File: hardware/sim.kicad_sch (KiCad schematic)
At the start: 8 parts, among them J14 Conn_01x06, J15 SIM_Card

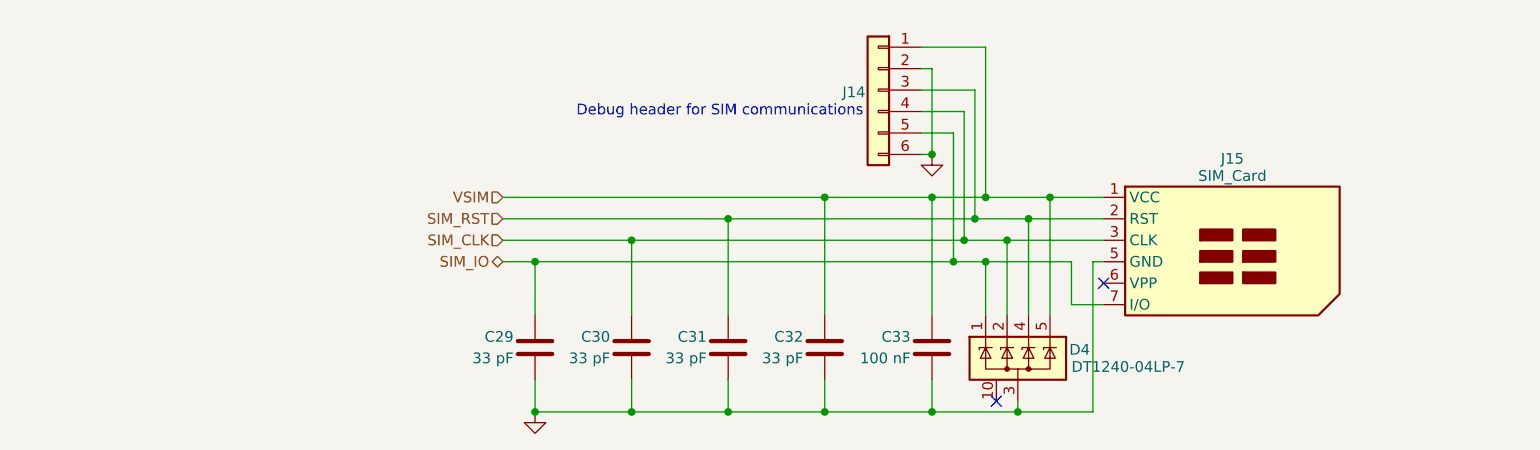
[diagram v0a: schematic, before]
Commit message: HW: Develop further
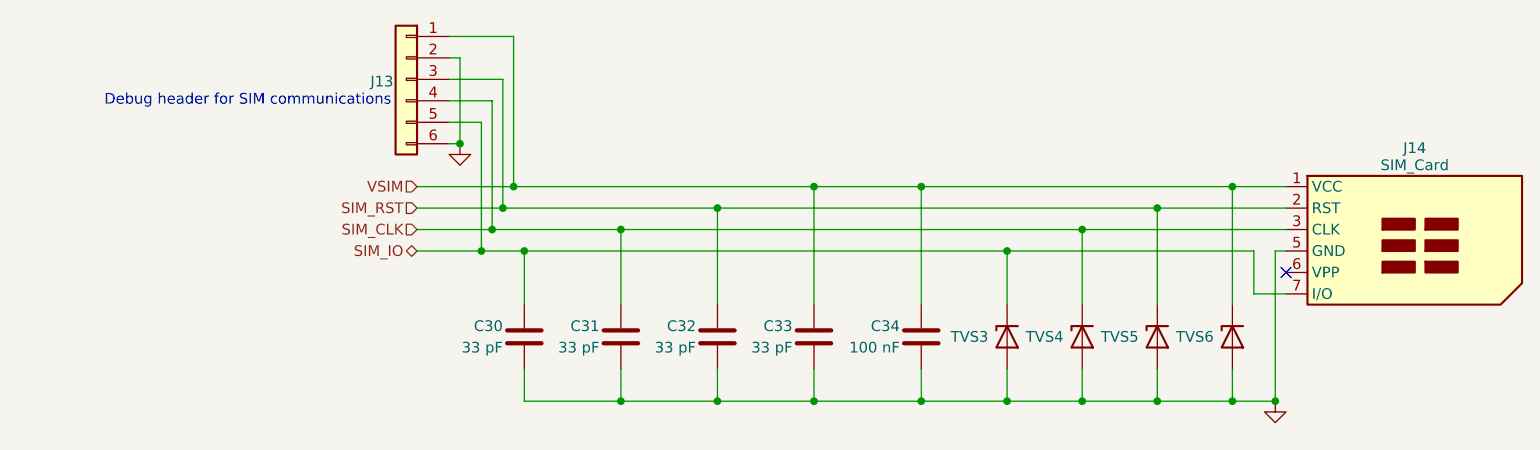
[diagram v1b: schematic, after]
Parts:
- removed D4: DT1240-04LP-7, Package_DFN_QFN:Diodes_UDFN-10_1.0x2.5mm_P0.5mm, symbol DT1240-04LP:DT1240-04LP
- added TVS3, TVS4, TVS5, TVS6: PE1605M1Q_R1_00001, Diode_SMD:D_0402_1005Metric, symbol Device:D_Zener
- renumbered C29 to C30, C30 to C31, C31 to C32, C32 to C33, C33 to C34, J14 to J13, J15 to J14
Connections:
- net GND: now also TVS3.2 (A), TVS4.2 (A), TVS5.2 (A), TVS6.2 (A)
- net SIM_CLK: now also TVS4.1 (K)
- net SIM_IO: now also TVS3.1 (K)
- net SIM_RST: now also TVS5.1 (K)
- net VSIM: now also TVS6.1 (K)
- no-connect marks 2 -> 1
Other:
- moved on the sheet: C30, C31, C32, C33, C34, J13, J14

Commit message: HW: Layout SIM section
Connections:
- net GND: now also J13.5 (Pin_5); no longer J13.6 (Pin_6)
- net SIM_CLK: now also J13.6 (Pin_6); no longer J13.4 (Pin_4)
- net SIM_IO: now also J13.4 (Pin_4); no longer J13.5 (Pin_5)
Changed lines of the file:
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@@
 	)
 	(junction
+		(at 92.71 111.76)
+		(diameter 0)
+		(color 0 0 0 0)
+	)
+	(junction
 		(at 146.05 144.78)
 		(diameter 0)
@@
 	)
 	(junction
-		(at 110.49 144.78)
+		(at 99.06 144.78)
 		(diameter 0)
 		(color 0 0 0 0)
 	)
 	(junction
-		(at 156.21 127)
+		(at 110.49 144.78)
 		(diameter 0)
 		(color 0 0 0 0)
 	)
 	(junction
-		(at 93.98 127)
+		(at 156.21 127)
 		(diameter 0)
 		(color 0 0 0 0)
@@
 	)
 	(junction
-		(at 96.52 121.92)
+		(at 182.88 144.78)
 		(diameter 0)
 		(color 0 0 0 0)
 	)
 	(junction
-		(at 91.44 114.3)
+		(at 97.79 121.92)
 		(diameter 0)
 		(color 0 0 0 0)
 	)
 	(junction
-		(at 182.88 144.78)
+		(at 100.33 119.38)
 		(diameter 0)
 		(color 0 0 0 0)
 	)
 	(junction
-		(at 133.35 144.78)
+		(at 95.25 127)
 		(diameter 0)
 		(color 0 0 0 0)
 	)
 	(junction
-		(at 182.88 119.38)
+		(at 133.35 144.78)
 		(diameter 0)
 		(color 0 0 0 0)
 	)
 	(junction
-		(at 95.25 124.46)
+		(at 182.88 119.38)
 		(diameter 0)
 		(color 0 0 0 0)
 	)
 	(junction
-		(at 97.79 119.38)
+		(at 90.17 124.46)
 		(diameter 0)
 		(color 0 0 0 0)
@@
 	(wire
 		(pts
-			(xy 121.92 121.92) (xy 173.99 121.92)
+			(xy 97.79 106.68) (xy 97.79 121.92)
 		)
 		(stroke
@@
 	(wire
 		(pts
-			(xy 95.25 109.22) (xy 95.25 124.46)
+			(xy 121.92 121.92) (xy 173.99 121.92)
 		)
 		(stroke
@@
 	(wire
 		(pts
-			(xy 96.52 106.68) (xy 96.52 121.92)
+			(xy 92.71 144.78) (xy 99.06 144.78)
 		)
 		(stroke
@@
 	(wire
 		(pts
-			(xy 91.44 104.14) (xy 91.44 114.3)
+			(xy 90.17 106.68) (xy 97.79 106.68)
 		)
 		(stroke
@@
 	(wire
 		(pts
-			(xy 97.79 119.38) (xy 133.35 119.38)
+			(xy 86.36 127) (xy 95.25 127)
 		)
 		(stroke
@@
 	(wire
 		(pts
+			(xy 90.17 114.3) (xy 90.17 124.46)
+		)
+		(stroke
+			(width 0)
+			(type default)
+		)
+	)
+	(wire
+		(pts
 			(xy 146.05 119.38) (xy 182.88 119.38)
 		)
@@
 	(wire
 		(pts
-			(xy 93.98 111.76) (xy 90.17 111.76)
+			(xy 86.36 119.38) (xy 100.33 119.38)
 		)
 		(stroke
@@
 	(wire
 		(pts
-			(xy 96.52 106.68) (xy 90.17 106.68)
+			(xy 156.21 140.97) (xy 156.21 144.78)
 		)
 		(stroke
@@
 	(wire
 		(pts
-			(xy 156.21 140.97) (xy 156.21 144.78)
+			(xy 173.99 121.92) (xy 189.23 121.92)
 		)
 		(stroke
@@
 	(wire
 		(pts
-			(xy 173.99 121.92) (xy 189.23 121.92)
+			(xy 100.33 101.6) (xy 100.33 119.38)
 		)
 		(stroke
@@
 	(wire
 		(pts
-			(xy 97.79 101.6) (xy 97.79 119.38)
+			(xy 99.06 127) (xy 156.21 127)
 		)
 		(stroke
@@
 	(wire
 		(pts
-			(xy 99.06 127) (xy 156.21 127)
+			(xy 173.99 121.92) (xy 173.99 133.35)
 		)
 		(stroke
@@
 	(wire
 		(pts
-			(xy 173.99 121.92) (xy 173.99 133.35)
+			(xy 182.88 119.38) (xy 189.23 119.38)
 		)
 		(stroke
@@
 	(wire
 		(pts
-			(xy 182.88 119.38) (xy 189.23 119.38)
+			(xy 100.33 119.38) (xy 133.35 119.38)
 		)
 		(stroke
@@
 	(wire
 		(pts
-			(xy 99.06 140.97) (xy 99.06 144.78)
+			(xy 86.36 124.46) (xy 90.17 124.46)
 		)
 		(stroke
@@
 	(wire
 		(pts
-			(xy 93.98 111.76) (xy 93.98 127)
+			(xy 99.06 140.97) (xy 99.06 144.78)
 		)
 		(stroke
@@
 	(wire
 		(pts
-			(xy 189.23 127) (xy 187.96 127)
+			(xy 95.25 109.22) (xy 95.25 127)
 		)
 		(stroke
@@
 	(wire
 		(pts
-			(xy 86.36 124.46) (xy 95.25 124.46)
+			(xy 92.71 111.76) (xy 92.71 144.78)
 		)
 		(stroke
@@
 	(wire
 		(pts
-			(xy 121.92 121.92) (xy 121.92 133.35)
+			(xy 189.23 127) (xy 187.96 127)
 		)
 		(stroke
@@
 	(wire
 		(pts
-			(xy 185.42 132.08) (xy 189.23 132.08)
+			(xy 90.17 111.76) (xy 92.71 111.76)
 		)
 		(stroke
@@
 	(wire
 		(pts
-			(xy 182.88 119.38) (xy 182.88 133.35)
+			(xy 90.17 104.14) (xy 92.71 104.14)
 		)
 		(stroke
@@
 	(wire
 		(pts
-			(xy 110.49 124.46) (xy 165.1 124.46)
+			(xy 121.92 121.92) (xy 121.92 133.35)
 		)
 		(stroke
@@
 	(wire
 		(pts
-			(xy 182.88 144.78) (xy 187.96 144.78)
+			(xy 185.42 132.08) (xy 189.23 132.08)
 		)
 		(stroke
@@
 	(wire
 		(pts
-			(xy 156.21 127) (xy 156.21 133.35)
+			(xy 90.17 109.22) (xy 95.25 109.22)
 		)
 		(stroke
@@
 	(wire
 		(pts
-			(xy 90.17 104.14) (xy 91.44 104.14)
+			(xy 182.88 119.38) (xy 182.88 133.35)
 		)
 		(stroke
@@
 	(wire
 		(pts
-			(xy 91.44 114.3) (xy 90.17 114.3)
+			(xy 110.49 124.46) (xy 165.1 124.46)
 		)
 		(stroke
@@
 	(wire
 		(pts
-			(xy 86.36 119.38) (xy 97.79 119.38)
+			(xy 182.88 144.78) (xy 187.96 144.78)
 		)
 		(stroke
@@
 	(wire
 		(pts
-			(xy 95.25 109.22) (xy 90.17 109.22)
+			(xy 156.21 127) (xy 156.21 133.35)
 		)
 		(stroke
@@
 	(wire
 		(pts
-			(xy 165.1 144.78) (xy 173.99 144.78)
+			(xy 92.71 104.14) (xy 92.71 111.76)
 		)
 		(stroke
@@
 	(wire
 		(pts
-			(xy 133.35 140.97) (xy 133.35 144.78)
+			(xy 97.79 121.92) (xy 121.92 121.92)
 		)
 		(stroke
@@
 	(wire
 		(pts
-			(xy 133.35 144.78) (xy 146.05 144.78)
+			(xy 165.1 144.78) (xy 173.99 144.78)
 		)
 		(stroke
@@
 	(wire
 		(pts
-			(xy 86.36 127) (xy 93.98 127)
+			(xy 90.17 101.6) (xy 100.33 101.6)
 		)
 		(stroke
@@
 	(wire
 		(pts
-			(xy 173.99 140.97) (xy 173.99 144.78)
+			(xy 133.35 140.97) (xy 133.35 144.78)
 		)
 		(stroke
@@
 	(wire
 		(pts
-			(xy 96.52 121.92) (xy 121.92 121.92)
+			(xy 133.35 144.78) (xy 146.05 144.78)
 		)
 		(stroke
@@
 	(wire
 		(pts
-			(xy 165.1 124.46) (xy 189.23 124.46)
+			(xy 173.99 140.97) (xy 173.99 144.78)
 		)
 		(stroke
@@
 	(wire
 		(pts
-			(xy 93.98 127) (xy 99.06 127)
+			(xy 165.1 124.46) (xy 189.23 124.46)
 		)
 		(stroke
@@
 	(wire
 		(pts
-			(xy 182.88 140.97) (xy 182.88 144.78)
+			(xy 95.25 127) (xy 99.06 127)
 		)
 		(stroke
@@
 	(wire
 		(pts
-			(xy 110.49 140.97) (xy 110.49 144.78)
+			(xy 182.88 140.97) (xy 182.88 144.78)
 		)
 		(stroke
@@
 	(wire
 		(pts
-			(xy 86.36 121.92) (xy 96.52 121.92)
+			(xy 90.17 124.46) (xy 110.49 124.46)
 		)
 		(stroke
@@
 	(wire
 		(pts
-			(xy 90.17 101.6) (xy 97.79 101.6)
+			(xy 110.49 140.97) (xy 110.49 144.78)
 		)
 		(stroke
@@
 	(wire
 		(pts
-			(xy 95.25 124.46) (xy 110.49 124.46)
+			(xy 86.36 121.92) (xy 97.79 121.92)
 		)
 		(stroke
@@
 					(unit 1)
 				)
-			)
-		)
-	)
-	(symbol
-		(lib_id "power:GND")
-		(at 91.44 114.3 0)
-		(unit 1)
-		(exclude_from_sim no)
-		(in_bom yes)
-		(on_board yes)
-		(dnp no)
-		(fields_autoplaced yes)
-		(property "Reference" "#PWR027"
-			(at 91.44 120.65 0)
-			(effects
-				(font
-					(size 1.27 1.27)
-				)
-				(hide yes)
-			)
-		)
-		(property "Value" "GND"
-			(at 91.44 119.38 0)
-			(effects
-				(font
-					(size 1.27 1.27)
-				)
-				(hide yes)
-			)
-		)
-		(property "Footprint" ""
-			(at 91.44 114.3 0)
-			(effects
-				(font
-					(size 1.27 1.27)
-				)
-				(hide yes)
-			)
-		)
-		(property "Datasheet" ""
-			(at 91.44 114.3 0)
-			(effects
-				(font
-					(size 1.27 1.27)
-				)
-				(hide yes)
-			)
-		)
-		(property "Description" "Power symbol creates a global label with name \"GND\" , ground"
-			(at 91.44 114.3 0)
-			(effects
-				(font
-					(size 1.27 1.27)
-				)
-				(hide yes)
-			)
-		)
-		(pin "1"
-		)
-		(instances
-			(project "iida_devkit"
-				(path "/b12a6e25-97fb-4aba-bc96-af8db389bb9a/33580d9f-a609-4568-baaf-9a29cf2dabcd"
-					(reference "#PWR027")
-					(unit 1)
-				)

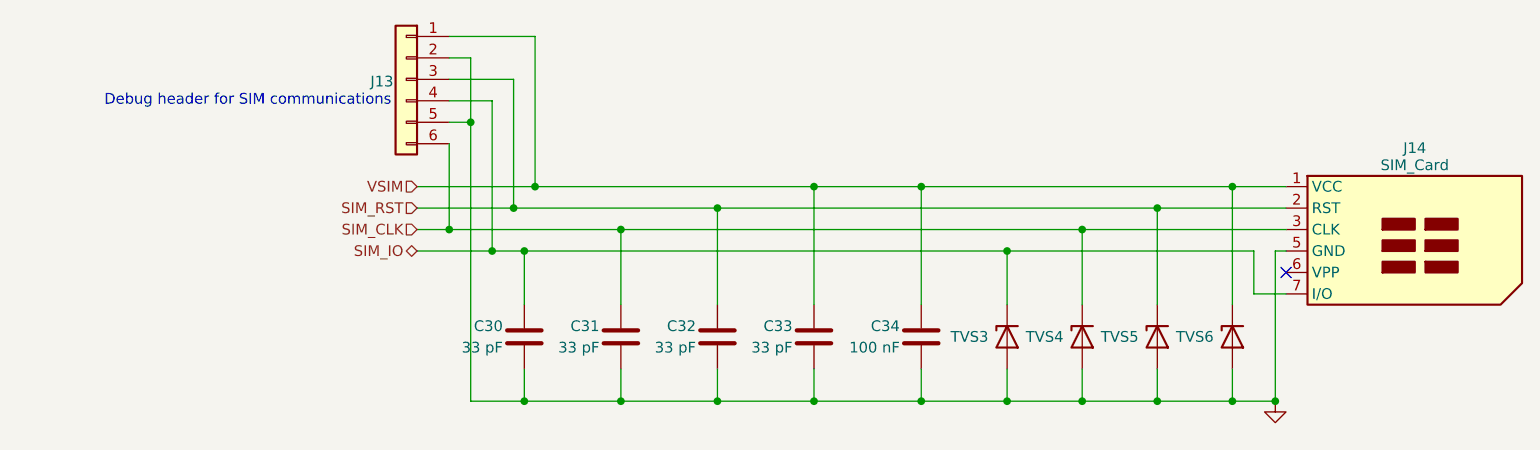
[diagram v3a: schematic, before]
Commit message: HW: Rework power section
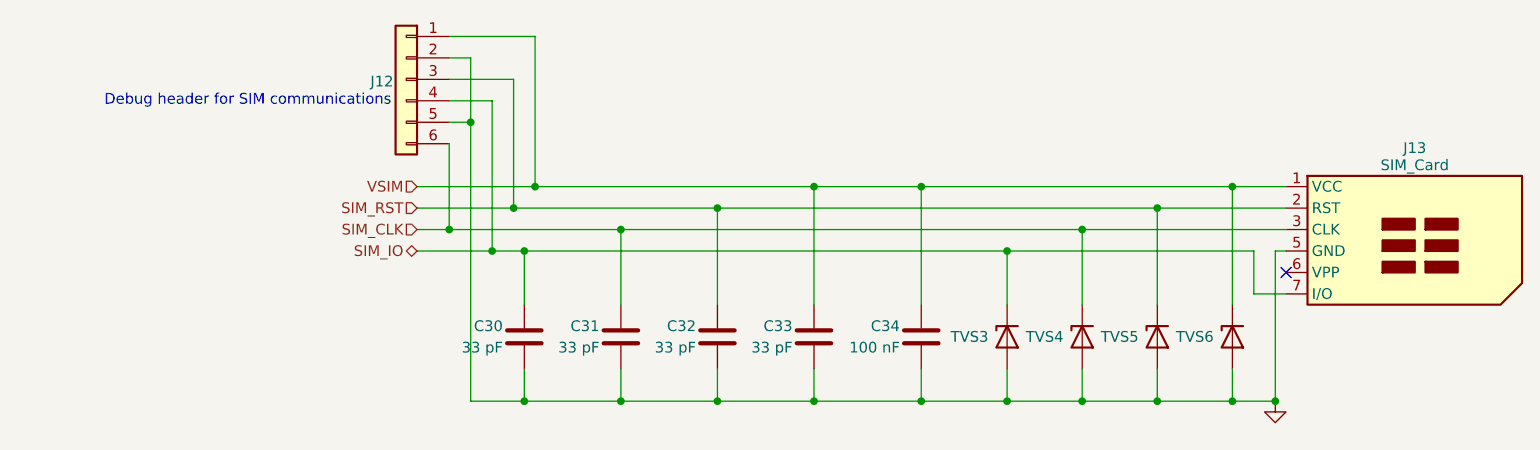
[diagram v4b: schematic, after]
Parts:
- renumbered J13 to J12, J14 to J13
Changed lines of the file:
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@@
 		(on_board yes)
 		(dnp no)
-		(property "Reference" "J13"
+		(property "Reference" "J12"
 			(at 83.566 106.934 0)
 			(effects
@@
 			(project "iida_devkit"
 				(path "/b12a6e25-97fb-4aba-bc96-af8db389bb9a/33580d9f-a609-4568-baaf-9a29cf2dabcd"
-					(reference "J13")
+					(reference "J12")
 					(unit 1)
 				)
@@
 		(on_board yes)
 		(dnp no)
-		(property "Reference" "J14"
+		(property "Reference" "J13"
 			(at 204.47 114.808 0)
 			(effects
@@
 			(project "iida_devkit"
 				(path "/b12a6e25-97fb-4aba-bc96-af8db389bb9a/33580d9f-a609-4568-baaf-9a29cf2dabcd"
-					(reference "J14")
+					(reference "J13")
 					(unit 1)
 				)
@@
 		(dnp no)
 		(fields_autoplaced yes)
-		(property "Reference" "#PWR027"
+		(property "Reference" "#PWR026"
 			(at 187.96 151.13 0)
 			(effects
@@
 			(project "iida_devkit"
 				(path "/b12a6e25-97fb-4aba-bc96-af8db389bb9a/33580d9f-a609-4568-baaf-9a29cf2dabcd"
-					(reference "#PWR027")
+					(reference "#PWR026")
 					(unit 1)
 				)

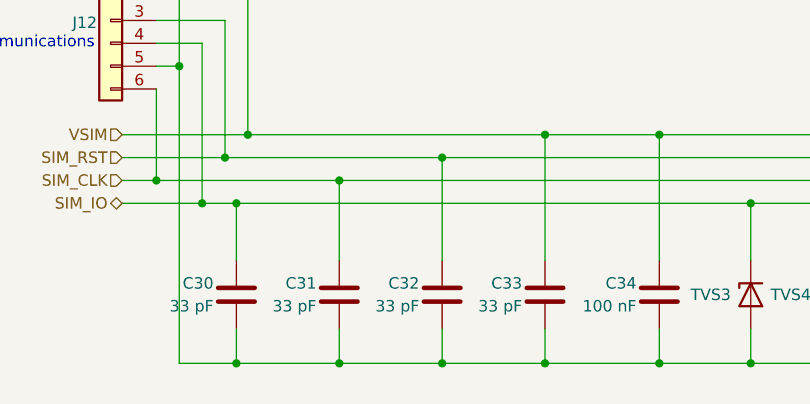
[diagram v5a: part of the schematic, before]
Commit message: HW: Update schematic
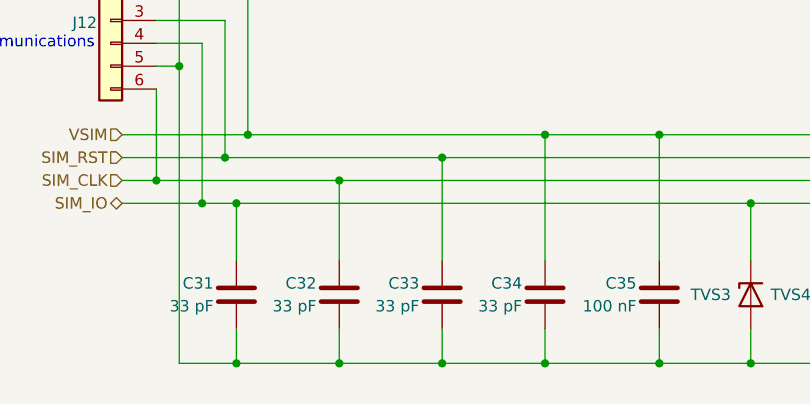
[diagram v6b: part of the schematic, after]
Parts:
- renumbered C30 to C31, C31 to C32, C32 to C33, C33 to C34, C34 to C35
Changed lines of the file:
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@@
 		(on_board yes)
 		(dnp no)
-		(property "Reference" "C34"
+		(property "Reference" "C35"
 			(at 143.51 135.89 0)
 			(effects
@@
 			(project "iida_devkit"
 				(path "/b12a6e25-97fb-4aba-bc96-af8db389bb9a/33580d9f-a609-4568-baaf-9a29cf2dabcd"
-					(reference "C34")
+					(reference "C35")
 					(unit 1)
 				)
@@
 		(on_board yes)
 		(dnp no)
-		(property "Reference" "C31"
+		(property "Reference" "C32"
 			(at 107.95 135.89 0)
 			(effects
@@
 			(project "iida_devkit"
 				(path "/b12a6e25-97fb-4aba-bc96-af8db389bb9a/33580d9f-a609-4568-baaf-9a29cf2dabcd"
-					(reference "C31")
+					(reference "C32")
 					(unit 1)
 				)
@@
 		(on_board yes)
 		(dnp no)
-		(property "Reference" "C30"
+		(property "Reference" "C31"
 			(at 96.52 135.89 0)
 			(effects
@@
 			(project "iida_devkit"
 				(path "/b12a6e25-97fb-4aba-bc96-af8db389bb9a/33580d9f-a609-4568-baaf-9a29cf2dabcd"
-					(reference "C30")
+					(reference "C31")
 					(unit 1)
 				)
@@
 		(on_board yes)
 		(dnp no)
-		(property "Reference" "C32"
+		(property "Reference" "C33"
 			(at 119.38 135.89 0)
 			(effects
@@
 			(project "iida_devkit"
 				(path "/b12a6e25-97fb-4aba-bc96-af8db389bb9a/33580d9f-a609-4568-baaf-9a29cf2dabcd"
-					(reference "C32")
+					(reference "C33")
 					(unit 1)
 				)
@@
 		(on_board yes)
 		(dnp no)
-		(property "Reference" "C33"
+		(property "Reference" "C34"
 			(at 130.81 135.89 0)
 			(effects
@@
 			(project "iida_devkit"
 				(path "/b12a6e25-97fb-4aba-bc96-af8db389bb9a/33580d9f-a609-4568-baaf-9a29cf2dabcd"
-					(reference "C33")
-					(unit 1)
-				)
+					(reference "C34")
+					(unit 1)
+				)
